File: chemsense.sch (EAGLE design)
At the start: 7 parts, among them J1 FFC-32, M1 ARDUINO_R3_ICSP, U1 MCP3424T-E/ST

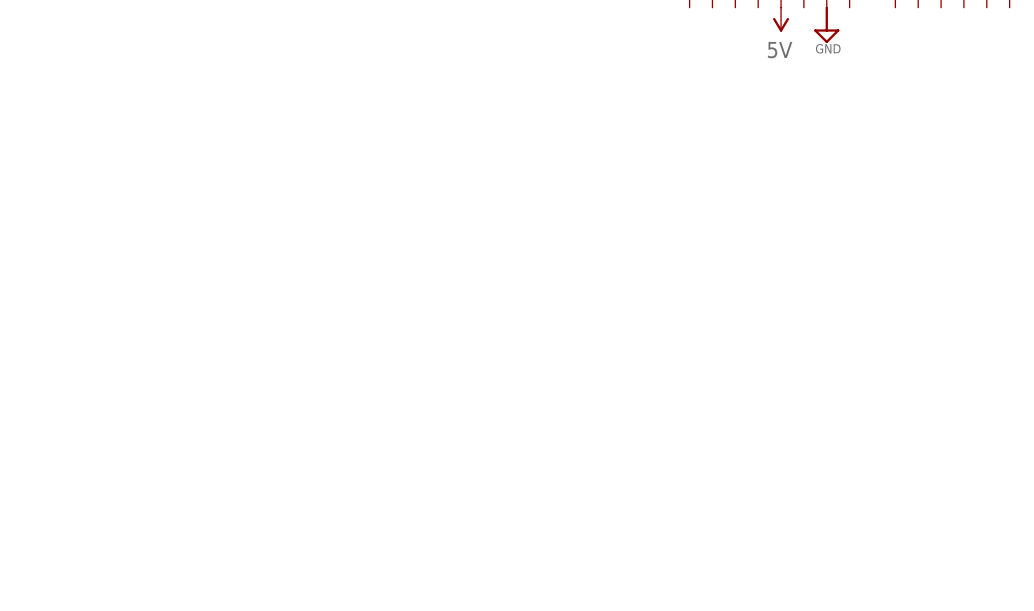
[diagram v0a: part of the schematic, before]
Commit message: add shrots for ref to gnd and electrodes
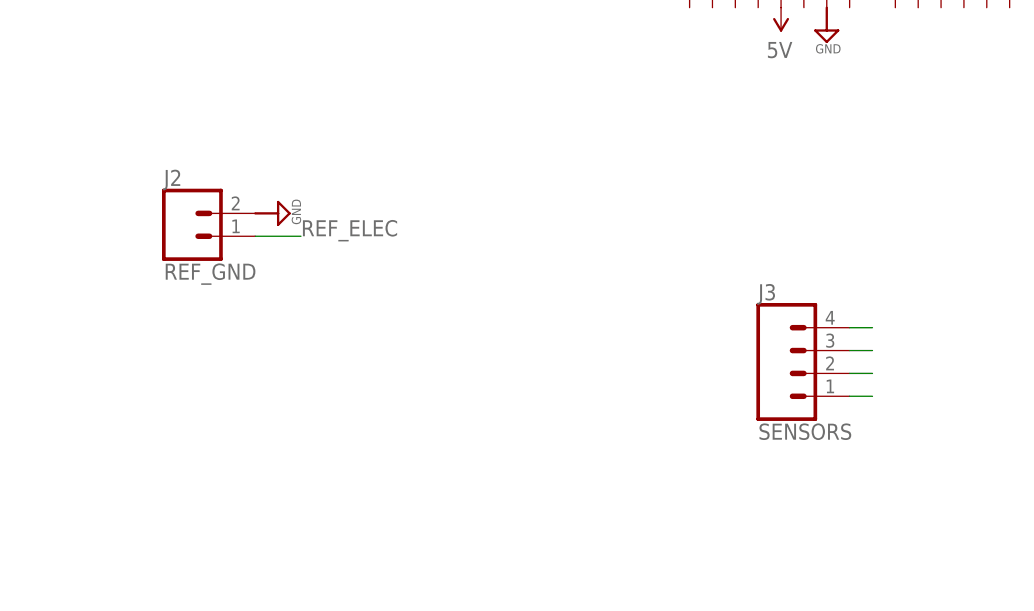
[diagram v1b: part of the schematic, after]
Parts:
- added J2: REF_GND, scono:CONN_02
- added J3: SENSORS, scono:CONN_04
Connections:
- new net N$1: J3.4
- new net N$2: J3.3
- new net N$3: J3.2
- new net N$4: J3.1
- new net REF_ELEC: J2.1
- net GND: now also J2.2
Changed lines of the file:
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@@
 <?xml version="1.0" encoding="utf-8"?>
 <!DOCTYPE eagle SYSTEM "eagle.dtd">
-<eagle version="9.5.1">
+<eagle version="9.5.2">
 <drawing>
 <settings>
@@
 <part name="SUPPLY5" library="scono" library_urn="urn:adsk.eagle:library:14850048" deviceset="GND" device=""/>
 <part name="U$6" library="scono" library_urn="urn:adsk.eagle:library:14850048" deviceset="5V" device=""/>
+<part name="J2" library="scono" library_urn="urn:adsk.eagle:library:14850048" deviceset="CONN_02" device="" package3d_urn="urn:adsk.eagle:package:38039/1" value="REF_GND"/>
+<part name="SUPPLY7" library="scono" library_urn="urn:adsk.eagle:library:14850048" deviceset="GND" device=""/>
+<part name="J3" library="scono" library_urn="urn:adsk.eagle:library:14850048" deviceset="CONN_04" device="" package3d_urn="urn:adsk.eagle:package:38085/1" value="SENSORS"/>
 </parts>
 <sheets>
@@
 <attribute name="VALUE" x="24.13" y="153.67" size="1.778" layer="96"/>
 </instance>
+<instance part="J2" gate="G$1" x="96.52" y="66.04" smashed="yes">
+<attribute name="VALUE" x="93.98" y="61.214" size="1.778" layer="96" font="vector"/>
+<attribute name="NAME" x="93.98" y="71.628" size="1.778" layer="95" font="vector"/>
+</instance>
+<instance part="SUPPLY7" gate="GND" x="106.68" y="68.58" smashed="yes" rot="R90">
+<attribute name="VALUE" x="109.22" y="67.31" size="1.016" layer="96" rot="R90"/>
+</instance>
+<instance part="J3" gate="G$1" x="165.1" y="50.8" smashed="yes">
+<attribute name="VALUE" x="160.02" y="43.434" size="1.778" layer="96" font="vector"/>
+<attribute name="NAME" x="160.02" y="58.928" size="1.778" layer="95" font="vector"/>
+</instance>
 </instances>
 <busses>
@@
 <pinref part="SUPPLY5" gate="GND" pin="GND"/>
 </segment>
+<segment>
+<pinref part="J2" gate="G$1" pin="2"/>
+<pinref part="SUPPLY7" gate="GND" pin="GND"/>
+</segment>
 </net>
 <net name="SDA" class="0">
@@
 </segment>
 </net>
+<net name="REF_ELEC" class="0">
+<segment>
+<pinref part="J2" gate="G$1" pin="1"/>
+<wire x1="104.14" y1="66.04" x2="109.22" y2="66.04" width="0.1524" layer="91"/>
+<label x="109.22" y="66.04" size="1.778" layer="95"/>
+</segment>
+</net>
+<net name="N$1" class="0">
+<segment>
+<pinref part="J3" gate="G$1" pin="4"/>
+<wire x1="170.18" y1="55.88" x2="172.72" y2="55.88" width="0.1524" layer="91"/>
+</segment>
+</net>
+<net name="N$2" class="0">
+<segment>
+<pinref part="J3" gate="G$1" pin="3"/>
+<wire x1="172.72" y1="53.34" x2="170.18" y2="53.34" width="0.1524" layer="91"/>
+</segment>
+</net>
+<net name="N$3" class="0">
+<segment>
+<pinref part="J3" gate="G$1" pin="2"/>
+<wire x1="172.72" y1="50.8" x2="170.18" y2="50.8" width="0.1524" layer="91"/>
+</segment>
+</net>
+<net name="N$4" class="0">
+<segment>
+<pinref part="J3" gate="G$1" pin="1"/>
+<wire x1="172.72" y1="48.26" x2="170.18" y2="48.26" width="0.1524" layer="91"/>
+</segment>
+</net>

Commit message: first board out and tested with diff firmware
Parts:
- removed R1: (no value), scono:R-US_0603
- added J4: I2C, scono:CONN_02
- added J5: GND, scono:CONN_02
- added J6: VDD, scono:CONN_02
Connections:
- removed net CH1+: U1.CH1+
- removed net CH1-: U1.CH1-
- removed net CH2+: U1.CH2+
- removed net CH2-: U1.CH2-
- removed net CH3+: U1.CH3+
- removed net CH3-: U1.CH3-
- removed net N$1: J3.4
- removed net N$2: J3.3
- removed net N$3: J3.2
- removed net N$4: J3.1
- removed net THERM: R1.1, U1.CH4+
- new net K: J1.18, J1.19, J1.20, J1.21, J1.22, J3.3, U1.CH3+
- new net NA: J1.11, J1.12, J1.13, J1.14, J1.15, J3.2, U1.CH2+
- new net NH4: J1.4, J1.5, J1.6, J1.7, J1.8, J3.1, U1.CH1+
- net 5V: now also J6.1, J6.2; no longer R1.2
- net GND: now also J5.1, J5.2; no longer U1.CH4-
- net REF_ELEC: now also J1.25, J1.26, J1.27, J1.28, J1.29, J3.4, U1.CH1-, U1.CH2-, U1.CH3-
- net SCL: now also J4.1
- net SDA: now also J4.2
